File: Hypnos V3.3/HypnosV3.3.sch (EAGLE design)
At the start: 38 parts, among them Q1 DMN65D8L-7, Q2 DMN65D8L-7

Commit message: Hypnos V3.3 Update
Changed SD pin from GPIO10 to GPIO9 and removed extra capacitors from design
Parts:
- removed C2, C4: 100pF, resistor:C-USC0805
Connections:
- removed net N$11: CS.1, FEATHERWING.GPIO10, MS2.GPIO10
- new net 10: FEATHERWING.GPIO10, MS2.GPIO10
- net 9: now also CS.1
- net GND: no longer C2.2, C4.2
- net N$10: no longer C2.1
- net N$15: no longer C4.1
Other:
- moved on the sheet: CS
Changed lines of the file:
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@@
 <part name="Q1" library="eDNA" deviceset="NMOS" device="" package3d_urn="urn:adsk.eagle:package:13526746/1" value="DMN65D8L-7"/>
 <part name="Q2" library="eDNA" deviceset="NMOS" device="" package3d_urn="urn:adsk.eagle:package:13526746/1" value="DMN65D8L-7"/>
-<part name="C2" library="resistor" library_urn="urn:adsk.eagle:library:348" deviceset="C-US" device="C0805" package3d_urn="urn:adsk.eagle:package:23617/2" value="100pF"/>
-<part name="C4" library="resistor" library_urn="urn:adsk.eagle:library:348" deviceset="C-US" device="C0805" package3d_urn="urn:adsk.eagle:package:23617/2" value="100pF"/>
-<part name="GND16" library="supply1" library_urn="urn:adsk.eagle:library:371" deviceset="GND" device=""/>
-<part name="GND17" library="supply1" library_urn="urn:adsk.eagle:library:371" deviceset="GND" device=""/>
 <part name="D1" library="semicon-smd-ipc" library_urn="urn:adsk.eagle:library:353" deviceset="D-" device="SOD123" package3d_urn="urn:adsk.eagle:package:26308/2"/>
 <part name="5V" library="SparkFun-Jumpers" library_urn="urn:adsk.eagle:library:528" deviceset="JUMPER-SMT_2_NC_TRACE" device="_SILK" package3d_urn="urn:adsk.eagle:package:39281/1" value=""/>
@@
 <attribute name="VALUE" x="745.49" y="-546.1" size="1.778" layer="96"/>
 </instance>
-<instance part="CS" gate="G$1" x="683.26" y="-642.62" smashed="yes" grouprefs="MOSFET_CIRCUITRY">
-<attribute name="NAME" x="685.8" y="-642.62" size="1.778" layer="95" font="vector"/>
-<attribute name="VALUE" x="685.8" y="-643.128" size="1.778" layer="96" font="vector" align="top-left"/>
+<instance part="CS" gate="G$1" x="683.26" y="-645.16" smashed="yes" grouprefs="MOSFET_CIRCUITRY">
+<attribute name="NAME" x="685.8" y="-645.16" size="1.778" layer="95" font="vector"/>
+<attribute name="VALUE" x="685.8" y="-645.668" size="1.778" layer="96" font="vector" align="top-left"/>
 </instance>
 <instance part="B1" gate="G$1" x="718.82" y="-551.18" smashed="yes" rot="R90" grouprefs="REAL_TIME_CLOCK">
@@
 <attribute name="NAME" x="779.78" y="-627.38" size="1.778" layer="95"/>
 <attribute name="VALUE" x="779.78" y="-629.92" size="1.778" layer="96"/>
-</instance>
-<instance part="C2" gate="G$1" x="731.52" y="-617.22" smashed="yes">
-<attribute name="NAME" x="732.536" y="-616.585" size="1.778" layer="95"/>
-<attribute name="VALUE" x="732.536" y="-621.411" size="1.778" layer="96"/>
-</instance>
-<instance part="C4" gate="G$1" x="769.62" y="-617.22" smashed="yes">
-<attribute name="NAME" x="770.636" y="-616.585" size="1.778" layer="95"/>
-<attribute name="VALUE" x="770.636" y="-621.411" size="1.778" layer="96"/>
-</instance>
-<instance part="GND16" gate="1" x="731.52" y="-624.84" smashed="yes">
-<attribute name="VALUE" x="728.98" y="-627.38" size="1.778" layer="96"/>
-</instance>
-<instance part="GND17" gate="1" x="769.62" y="-624.84" smashed="yes">
-<attribute name="VALUE" x="767.08" y="-627.38" size="1.778" layer="96"/>
 </instance>
 <instance part="D1" gate="G$1" x="843.28" y="-553.72" smashed="yes" rot="R270" grouprefs="SDCARD">
@@
 <pinref part="GND15" gate="1" pin="GND"/>
 </segment>
-<segment>
-<pinref part="C2" gate="G$1" pin="2"/>
-<pinref part="GND16" gate="1" pin="GND"/>
-</segment>
-<segment>
-<pinref part="C4" gate="G$1" pin="2"/>
-<pinref part="GND17" gate="1" pin="GND"/>
-</segment>
 </net>
 <net name="DO" class="0">
@@
 <segment>
 <pinref part="CS" gate="G$1" pin="2"/>
-<wire x1="688.34" y1="-642.62" x2="701.04" y2="-642.62" width="0.1524" layer="91" grouprefs="MOSFET_CIRCUITRY"/>
-<label x="701.04" y="-642.62" size="1.778" layer="95" xref="yes" grouprefs="MOSFET_CIRCUITRY"/>
+<wire x1="688.34" y1="-645.16" x2="701.04" y2="-645.16" width="0.1524" layer="91" grouprefs="MOSFET_CIRCUITRY"/>
+<label x="701.04" y="-645.16" size="1.778" layer="95" xref="yes" grouprefs="MOSFET_CIRCUITRY"/>
 </segment>
 </net>
@@
 <pinref part="FEATHERWING" gate="G$1" pin="GPIO9"/>
 <wire x1="833.12" y1="-632.46" x2="828.04" y2="-632.46" width="0.1524" layer="91" grouprefs="CONTROLLED_LOGIC"/>
-<label x="828.04" y="-632.46" size="1.778" layer="95" grouprefs="CONTROLLED_LOGIC"/>
+<label x="828.04" y="-632.46" size="1.778" layer="95" rot="R180" xref="yes"/>
 </segment>
 <segment>
@@
 <wire x1="675.64" y1="-645.16" x2="678.18" y2="-645.16" width="0.1524" layer="91"/>
 <label x="678.18" y="-645.16" size="1.778" layer="95"/>
+<pinref part="CS" gate="G$1" pin="1"/>
 </segment>
 </net>
@@
 <pinref part="R4" gate="G$1" pin="1"/>
 <pinref part="Q1" gate="G$1" pin="D"/>
-<pinref part="C2" gate="G$1" pin="1"/>
-<wire x1="731.52" y1="-614.68" x2="739.14" y2="-614.68" width="0.1524" layer="91"/>
 </segment>
 </net>
@@
 </segment>
 </net>
-<net name="N$11" class="0">
-<segment>
-<pinref part="CS" gate="G$1" pin="1"/>
-<wire x1="678.18" y1="-642.62" x2="675.64" y2="-642.62" width="0.1524" layer="91" grouprefs="MOSFET_CIRCUITRY"/>
-<pinref part="MS2" gate="G$1" pin="GPIO10"/>
-</segment>
-<segment>
-<wire x1="833.12" y1="-629.92" x2="828.04" y2="-629.92" width="0.1524" layer="91" grouprefs="CONTROLLED_LOGIC"/>
-<label x="828.04" y="-629.92" size="1.778" layer="95" rot="R180" xref="yes" grouprefs="CONTROLLED_LOGIC"/>
-<pinref part="FEATHERWING" gate="G$1" pin="GPIO10"/>
-</segment>
-</net>
 <net name="N$14" class="0">
 <segment>
@@
 <junction x="777.24" y="-617.22" grouprefs="MOSFET_CIRCUITRY"/>
 <pinref part="Q2" gate="G$1" pin="D"/>
-<pinref part="C4" gate="G$1" pin="1"/>
-<wire x1="769.62" y1="-614.68" x2="774.7" y2="-614.68" width="0.1524" layer="91"/>
-<wire x1="774.7" y1="-614.68" x2="774.7" y2="-617.22" width="0.1524" layer="91"/>
-<wire x1="774.7" y1="-617.22" x2="777.24" y2="-617.22" width="0.1524" layer="91"/>
 </segment>
 </net>
@@
 </segment>
 </net>
+<net name="10" class="0">
+<segment>
+<pinref part="MS2" gate="G$1" pin="GPIO10"/>
+<wire x1="675.64" y1="-642.62" x2="680.72" y2="-642.62" width="0.1524" layer="91"/>
+<label x="678.18" y="-642.62" size="1.778" layer="95"/>
+</segment>
+<segment>
+<wire x1="833.12" y1="-629.92" x2="828.04" y2="-629.92" width="0.1524" layer="91" grouprefs="CONTROLLED_LOGIC"/>
+<pinref part="FEATHERWING" gate="G$1" pin="GPIO10"/>
+<label x="828.04" y="-629.92" size="1.778" layer="95"/>
+</segment>
+</net>

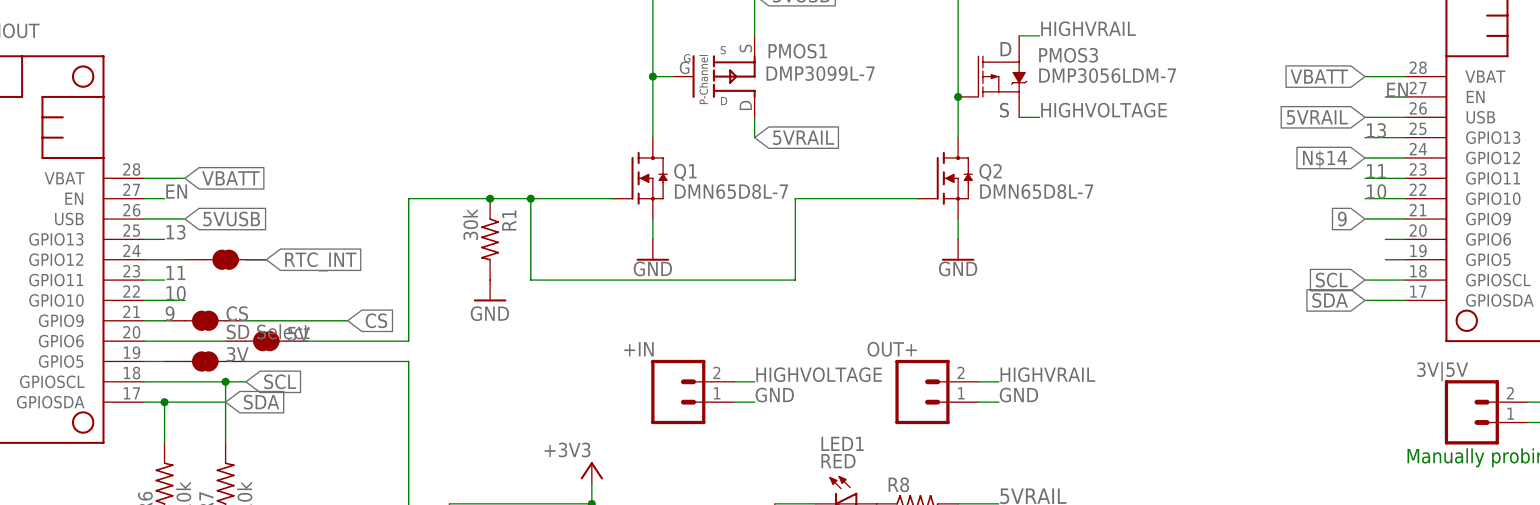
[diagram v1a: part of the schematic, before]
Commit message: Hypnos V3.3 Update
Switched SD pin from pin 9 to pin 11 due to Feather pin issues, updated BOM with in-stock parts from Digikey
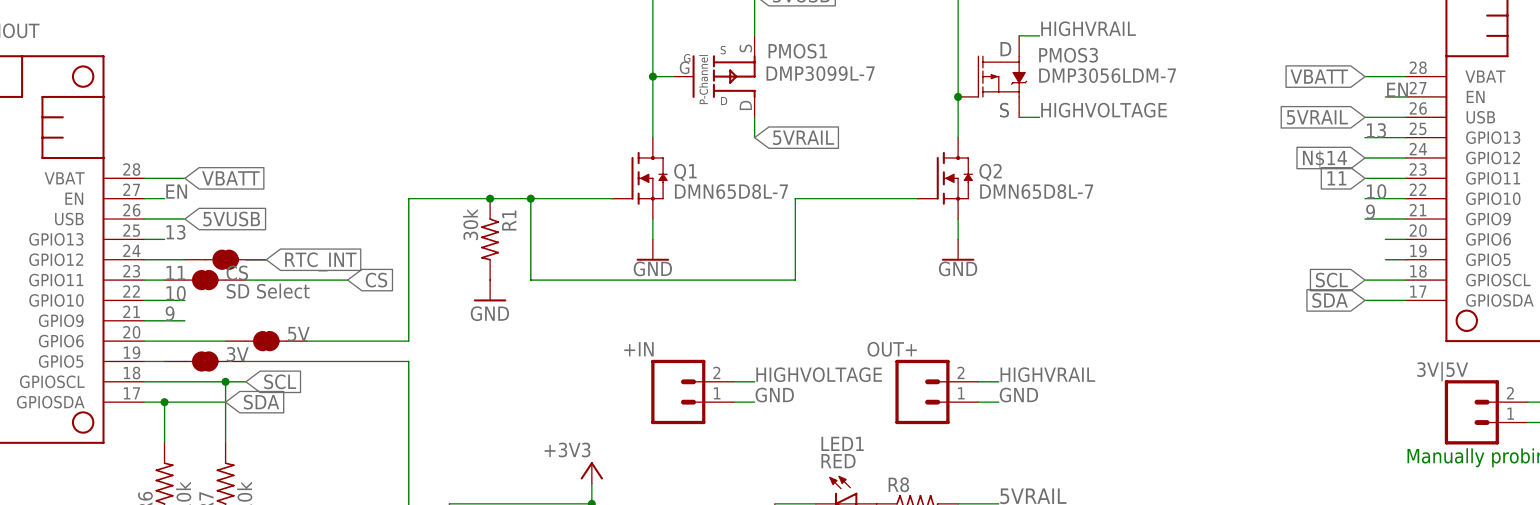
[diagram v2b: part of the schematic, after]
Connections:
- net 11: now also CS.1
- net 9: no longer CS.1
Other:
- moved on the sheet: CS
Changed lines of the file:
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@@
 <attribute name="VALUE" x="745.49" y="-546.1" size="1.778" layer="96"/>
 </instance>
-<instance part="CS" gate="G$1" x="683.26" y="-645.16" smashed="yes" grouprefs="MOSFET_CIRCUITRY">
-<attribute name="NAME" x="685.8" y="-645.16" size="1.778" layer="95" font="vector"/>
-<attribute name="VALUE" x="685.8" y="-645.668" size="1.778" layer="96" font="vector" align="top-left"/>
+<instance part="CS" gate="G$1" x="683.26" y="-640.08" smashed="yes" grouprefs="MOSFET_CIRCUITRY">
+<attribute name="NAME" x="685.8" y="-640.08" size="1.778" layer="95" font="vector"/>
+<attribute name="VALUE" x="685.8" y="-640.588" size="1.778" layer="96" font="vector" align="top-left"/>
 </instance>
 <instance part="B1" gate="G$1" x="718.82" y="-551.18" smashed="yes" rot="R90" grouprefs="REAL_TIME_CLOCK">
@@
 <segment>
 <pinref part="CS" gate="G$1" pin="2"/>
-<wire x1="688.34" y1="-645.16" x2="701.04" y2="-645.16" width="0.1524" layer="91" grouprefs="MOSFET_CIRCUITRY"/>
-<label x="701.04" y="-645.16" size="1.778" layer="95" xref="yes" grouprefs="MOSFET_CIRCUITRY"/>
+<wire x1="688.34" y1="-640.08" x2="701.04" y2="-640.08" width="0.1524" layer="91" grouprefs="MOSFET_CIRCUITRY"/>
+<label x="701.04" y="-640.08" size="1.778" layer="95" xref="yes" grouprefs="MOSFET_CIRCUITRY"/>
 </segment>
 </net>
@@
 <pinref part="FEATHERWING" gate="G$1" pin="GPIO9"/>
 <wire x1="833.12" y1="-632.46" x2="828.04" y2="-632.46" width="0.1524" layer="91" grouprefs="CONTROLLED_LOGIC"/>
-<label x="828.04" y="-632.46" size="1.778" layer="95" rot="R180" xref="yes"/>
+<label x="828.04" y="-632.46" size="1.778" layer="95"/>
 </segment>
 <segment>
 <pinref part="MS2" gate="G$1" pin="GPIO9"/>
-<wire x1="675.64" y1="-645.16" x2="678.18" y2="-645.16" width="0.1524" layer="91"/>
+<wire x1="675.64" y1="-645.16" x2="680.72" y2="-645.16" width="0.1524" layer="91"/>
 <label x="678.18" y="-645.16" size="1.778" layer="95"/>
-<pinref part="CS" gate="G$1" pin="1"/>
 </segment>
 </net>
@@
 <label x="678.18" y="-640.08" size="1.778" layer="95" grouprefs="MOSFET_CIRCUITRY"/>
 <pinref part="MS2" gate="G$1" pin="GPIO11"/>
+<pinref part="CS" gate="G$1" pin="1"/>
 </segment>
 <segment>
 <pinref part="FEATHERWING" gate="G$1" pin="GPIO11"/>
 <wire x1="833.12" y1="-627.38" x2="828.04" y2="-627.38" width="0.1524" layer="91" grouprefs="CONTROLLED_LOGIC"/>
-<label x="828.04" y="-627.38" size="1.778" layer="95" grouprefs="CONTROLLED_LOGIC"/>
-</segment>
-</net>
+<label x="828.04" y="-627.38" size="1.778" layer="95" rot="R180" xref="yes"/>
+</segment>
+</net>
